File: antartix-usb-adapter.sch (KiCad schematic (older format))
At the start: 118 parts, among them IC1 FT2232D, J1 QTE-020-04-L-D-A, J2 0022232041, J3 614004185023, J4 WE_629105150521, J5 614004185023, J6 614004185023, U1 PCT2075GVX, U2 PAC1934T-I_JQ, U3 USB2514B-I_M2, U4 TPS2024DR, U5 TPS2024DR, U6 TPS2024DR, Y1 7C-24.000MBB-T, Y2 MQ-6.000-12-30_30_

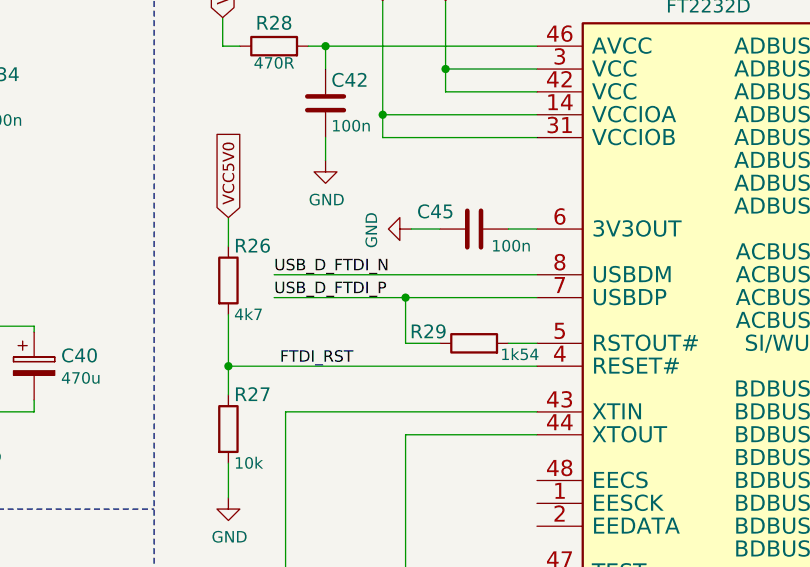
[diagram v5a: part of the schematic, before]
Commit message: Route console and HDMI control signals
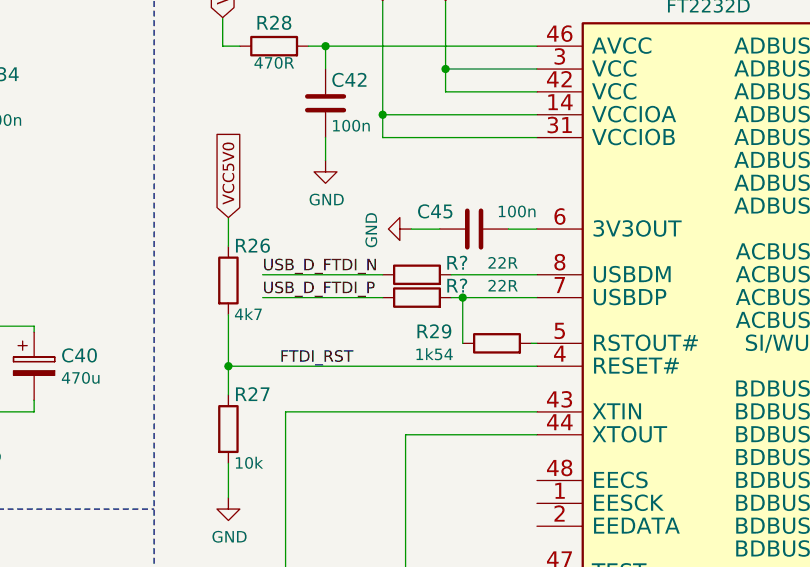
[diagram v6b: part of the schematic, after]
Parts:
- added R? (x2): R_22R_0402, antartix-arty-controller-footprints:0402-res, symbol antartix-arty-controller:R_22R_0402
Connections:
- net USB_D_FTDI_N: now also R?.1; no longer IC1.8 (USBDM)
- net USB_D_FTDI_P: now also R?.1; no longer IC1.7 (USBDP), R29.1
- new net: IC1.8 (USBDM), R?.2
- new net: IC1.7 (USBDP), R29.1, R?.2
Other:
- moved on the sheet: R29
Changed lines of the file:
@@
 $EndComp
 Wire Wire Line
-	12800 7650 12650 7650
-Wire Wire Line
-	12650 7450 12075 7450
-Connection ~ 12650 7450
-Wire Wire Line
-	12650 7650 12650 7450
-Wire Wire Line
-	13225 7650 13100 7650
+	13225 7650 13200 7650
 $Comp
 L antartix-arty-controller:R_1k54_0402 R?
 U 1 1 60939406
-P 12950 7650
+P 13050 7650
 AR Path="/60939406" Ref="R?"  Part="1"
 AR Path="/60924187/60939406" Ref="R29"  Part="1"
-F 0 "R29" H 12750 7700 60  0000 C CNN
-F 1 "R_1k54_0402" H 12950 7500 60  0001 C CNN
-F 2 "antartix-arty-controller-footprints:0402-res" H 13150 7850 60  0001 L CNN
-F 3 "" H 12950 7650 50  0001 C CNN
-F 4 "VISHAY" H 13150 8050 60  0001 L CNN "Manufacturer"
-F 5 "CRCW04021K54FKED." H 13150 7950 60  0001 L CNN "MPN"
-F 6 "1k54" H 13150 7600 50  0000 C CNN "Val"
-	1    12950 7650
+F 0 "R29" H 12775 7700 60  0000 C CNN
+F 1 "R_1k54_0402" H 13050 7500 60  0001 C CNN
+F 2 "antartix-arty-controller-footprints:0402-res" H 13250 7850 60  0001 L CNN
+F 3 "" H 13050 7650 50  0001 C CNN
+F 4 "VISHAY" H 13250 8050 60  0001 L CNN "Manufacturer"
+F 5 "CRCW04021K54FKED." H 13250 7950 60  0001 L CNN "MPN"
+F 6 "1k54" H 12775 7600 50  0000 C CNN "Val"
+	1    13050 7650
 	1    0    0    -1
 $EndComp
@@
 F 4 "Walsin" H 13150 7550 60  0001 L CNN "Manufacturer"
 F 5 "0402X104K6R3CT" H 13150 7450 60  0001 L CNN "MPN"
-F 6 "100n" V 13025 7225 50  0000 L CNN "Val"
+F 6 "100n" V 12875 7250 50  0000 L CNN "Val"
 	1    12950 7150
 	0    1    1    0
@@
 Wire Wire Line
 	14725 6450 14825 6450
-Text Label 12075 7450 0    50   ~ 0
+Text Label 12025 7450 0    50   ~ 0
 USB_D_FTDI_P
-Wire Wire Line
-	13225 7450 12650 7450
-Text Label 12075 7350 0    50   ~ 0
+Text Label 12025 7350 0    50   ~ 0
 USB_D_FTDI_N
-Wire Wire Line
-	13225 7350 12075 7350
 Text Label 15750 6650 2    50   ~ 0
 WP_FTDI
@@
 	1    0    0    -1
 $EndComp
+$Comp
+L antartix-arty-controller:R_22R_0402 R?
+U 1 1 605E94E5
+P 12700 7350
+AR Path="/604C47E1/605E94E5" Ref="R?"  Part="1"
+AR Path="/60924187/605E94E5" Ref="R?"  Part="1"
+F 0 "R?" H 12875 7400 60  0000 C CNN
+F 1 "R_22R_0402" H 12700 7200 60  0001 C CNN
+F 2 "antartix-arty-controller-footprints:0402-res" H 12900 7550 60  0001 L CNN
+F 3 "" H 12700 7350 50  0001 C CNN
+F 4 "VISHAY" H 12900 7750 60  0001 L CNN "Manufacturer"
+F 5 "CRCW040222R0FKED" H 12900 7650 60  0001 L CNN "MPN"
+F 6 "22R" H 13075 7400 50  0000 C CNN "Val"
+	1    12700 7350
+	1    0    0    -1
+$EndComp
+Wire Wire Line
+	12850 7450 12900 7450
+$Comp
+L antartix-arty-controller:R_22R_0402 R?
+U 1 1 605E94EE
+P 12700 7450
+AR Path="/604C47E1/605E94EE" Ref="R?"  Part="1"
+AR Path="/60924187/605E94EE" Ref="R?"  Part="1"
+F 0 "R?" H 12875 7500 60  0000 C CNN
+F 1 "R_22R_0402" H 12700 7300 60  0001 C CNN
+F 2 "antartix-arty-controller-footprints:0402-res" H 12900 7650 60  0001 L CNN
+F 3 "" H 12700 7450 50  0001 C CNN
+F 4 "VISHAY" H 12900 7850 60  0001 L CNN "Manufacturer"
+F 5 "CRCW040222R0FKED" H 12900 7750 60  0001 L CNN "MPN"
+F 6 "22R" H 13075 7500 50  0000 C CNN "Val"
+	1    12700 7450
+	1    0    0    -1
+$EndComp
+Wire Wire Line
+	12900 7650 12900 7450
+Connection ~ 12900 7450
+Wire Wire Line
+	12900 7450 13225 7450
+Wire Wire Line
+	12850 7350 13225 7350
+Wire Wire Line
+	12550 7350 12025 7350
+Wire Wire Line
+	12550 7450 12025 7450
 $EndSCHEMATC

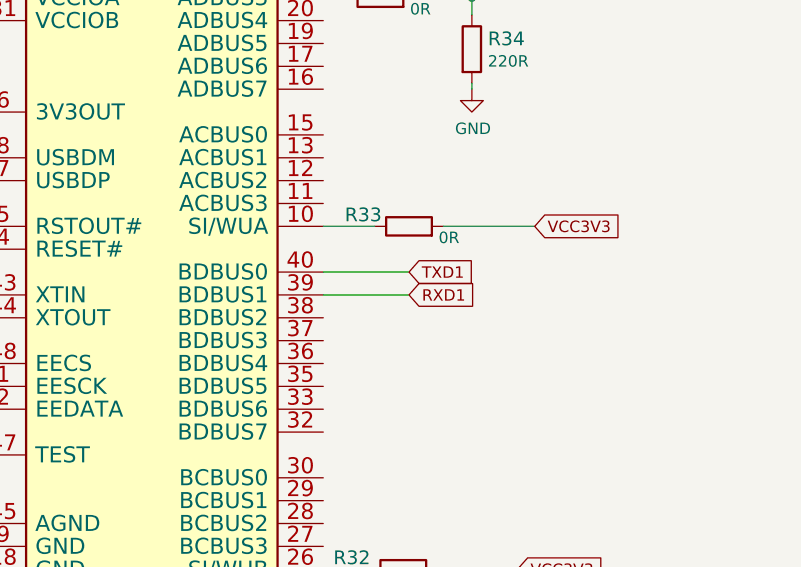
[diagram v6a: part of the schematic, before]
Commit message: Remove TXD1 and RXD1 labels
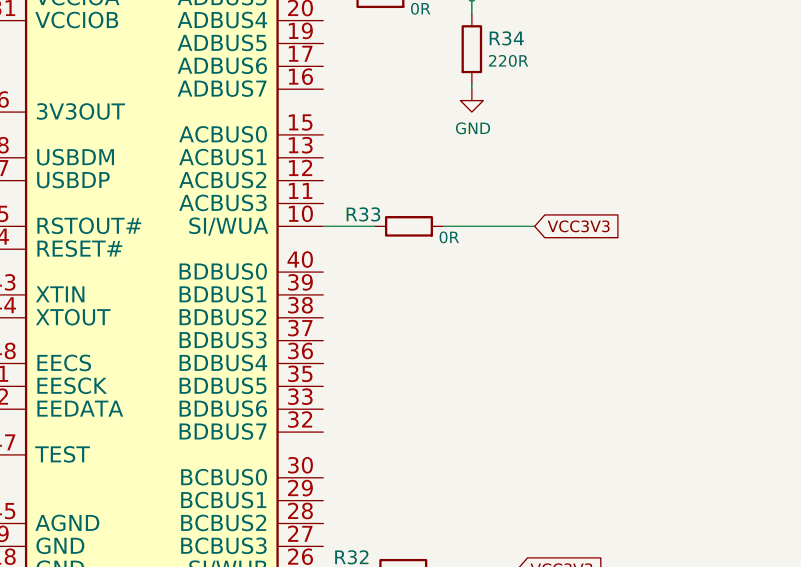
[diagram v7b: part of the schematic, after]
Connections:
- net RXD1: no longer names the net of IC1.39 (BDBUS1)
- net TXD1: no longer names the net of IC1.40 (BDBUS0)
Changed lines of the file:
@@
 	1    0    0    -1
 $EndComp
-Text GLabel 15100 7850 2    50   Input ~ 0
-TXD1
-Text GLabel 15100 7950 2    50   Input ~ 0
-RXD1
-Wire Wire Line
-	15100 7850 14725 7850
-Wire Wire Line
-	15100 7950 14725 7950
 Text GLabel 3200 2375 2    50   Input ~ 0
 USB1_EN

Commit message: Add local libraries
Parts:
- C10, C11, C12: footprint antmicro-footprints:0603-cap -> antartix-arty-controller-footprints:0603-cap; symbol antmicroCapacitors0603:C_100n_0603 -> antartix-arty-controller:C_100n_0603
- C13: footprint antmicro-footprints:0402-cap -> antartix-arty-controller-footprints:0402-cap; symbol antmicroCapacitors0402:C_1u_0402 -> antartix-arty-controller:C_1u_0402
- C37, C38, C39: footprint antmicro-footprints:0603-cap -> antartix-arty-controller-footprints:0603-cap; symbol antmicroCapacitors0603:C_22u_0603 -> antartix-arty-controller:C_22u_0603
- J2: footprint antmicro-footprints:PinHeader_1x4_P2.54mm_Drill1.02mm -> antartix-arty-controller-footprints:PinHeader_1x4_P2.54mm_Drill1.02mm
- J3, J5, J6: symbol antmicroUSBDVIHDMIConnectors:614004185023 -> antartix-arty-controller:614004185023
- N1: footprint antmicro-footprints:antmicro-logo_scaled_15mm -> antartix-arty-controller-footprints:antmicro-logo_scaled_15mm; symbol antmicroMechanicalParts:antmicro_logo -> antartix-arty-controller:antmicro_logo
- N2: footprint antmicro-footprints:oshw-logo -> antartix-arty-controller-footprints:oshw-logo; symbol antmicroMechanicalParts:oshw_logo -> antartix-arty-controller:oshw_logo
- R25: footprint antmicro-footprints:0402-res -> antartix-arty-controller-footprints:0402-res; symbol antmicroResistors0402:R_12k_0402 -> antartix-arty-controller:R_12k_0402
- R3, R4: footprint antmicro-footprints:0805-res -> antartix-arty-controller-footprints:0805-res; symbol antmicroResistorsmisc:R_0R_0805 -> antartix-arty-controller:R_0R_0805
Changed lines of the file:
@@
 F 0 "J2" V 6925 7308 50  0000 C CNN
 F 1 "0022232041" V 7016 7308 50  0000 C CNN
-F 2 "antmicro-footprints:PinHeader_1x4_P2.54mm_Drill1.02mm" H 7350 7500 60  0001 L CNN
+F 2 "antartix-arty-controller-footprints:PinHeader_1x4_P2.54mm_Drill1.02mm" H 7350 7500 60  0001 L CNN
 F 3 "https://www.molex.com/pdm_docs/sd/022232041_sd.pdf" H 7350 7600 60  0001 L CNN
 F 4 "0022232041" H 7350 7800 60  0001 L CNN "MPN"
@@
 VCC3V3
 $Comp
-L antmicroCapacitors0402:C_1u_0402 C?
+L antartix-arty-controller:C_1u_0402 C?
 U 1 1 60938EAE
 P 9000 6575
@@
 F 0 "C13" H 9025 6675 60  0000 L CNN
 F 1 "C_1u_0402" H 9000 6425 60  0001 C CNN
-F 2 "antmicro-footprints:0402-cap" H 9200 6775 60  0001 L CNN
+F 2 "antartix-arty-controller-footprints:0402-cap" H 9200 6775 60  0001 L CNN
 F 3 "" H 9000 6575 50  0001 C CNN
 F 4 "TDK" H 9200 6975 60  0001 L CNN "Manufacturer"
@@
 $EndComp
 $Comp
-L antmicroCapacitors0603:C_100n_0603 C?
+L antartix-arty-controller:C_100n_0603 C?
 U 1 1 60938F63
 P 9000 3550
@@
 F 0 "C12" H 8775 3625 60  0000 L CNN
 F 1 "C_100n_0603" H 9000 3400 60  0001 C CNN
-F 2 "antmicro-footprints:0603-cap" H 9200 3750 60  0001 L CNN
+F 2 "antartix-arty-controller-footprints:0603-cap" H 9200 3750 60  0001 L CNN
 F 3 "" H 9000 3550 50  0001 C CNN
 F 4 "AVX" H 9200 3950 60  0001 L CNN "Manufacturer"
@@
 $EndComp
 $Comp
-L antmicroCapacitors0603:C_22u_0603 C?
+L antartix-arty-controller:C_22u_0603 C?
 U 1 1 60938F8D
 P 10975 3500
@@
 F 0 "C39" H 10775 3400 60  0000 L CNN
 F 1 "C_22u_0603" H 10975 3350 60  0001 C CNN
-F 2 "antmicro-footprints:0603-cap" H 11175 3700 60  0001 L CNN
+F 2 "antartix-arty-controller-footprints:0603-cap" H 11175 3700 60  0001 L CNN
 F 3 "" H 10975 3500 50  0001 C CNN
 F 4 "MURATA" H 11175 3900 60  0001 L CNN "Manufacturer"
@@
 $EndComp
 $Comp
-L antmicroCapacitors0603:C_100n_0603 C?
+L antartix-arty-controller:C_100n_0603 C?
 U 1 1 60938FAF
 P 9000 2525
@@
 F 0 "C11" H 8775 2600 60  0000 L CNN
 F 1 "C_100n_0603" H 9000 2375 60  0001 C CNN
-F 2 "antmicro-footprints:0603-cap" H 9200 2725 60  0001 L CNN
+F 2 "antartix-arty-controller-footprints:0603-cap" H 9200 2725 60  0001 L CNN
 F 3 "" H 9000 2525 50  0001 C CNN
 F 4 "AVX" H 9200 2925 60  0001 L CNN "Manufacturer"
@@
 $EndComp
 $Comp
-L antmicroCapacitors0603:C_22u_0603 C?
+L antartix-arty-controller:C_22u_0603 C?
 U 1 1 60938FD9
 P 10975 2475
@@
 F 0 "C38" H 10775 2375 60  0000 L CNN
 F 1 "C_22u_0603" H 10975 2325 60  0001 C CNN
-F 2 "antmicro-footprints:0603-cap" H 11175 2675 60  0001 L CNN
+F 2 "antartix-arty-controller-footprints:0603-cap" H 11175 2675 60  0001 L CNN
 F 3 "" H 10975 2475 50  0001 C CNN
 F 4 "MURATA" H 11175 2875 60  0001 L CNN "Manufacturer"
@@
 $EndComp
 $Comp
-L antmicroCapacitors0603:C_100n_0603 C?
+L antartix-arty-controller:C_100n_0603 C?
 U 1 1 60938FFC
 P 9000 1525
@@
 F 0 "C10" H 8775 1600 60  0000 L CNN
 F 1 "C_100n_0603" H 9000 1375 60  0001 C CNN
-F 2 "antmicro-footprints:0603-cap" H 9200 1725 60  0001 L CNN
+F 2 "antartix-arty-controller-footprints:0603-cap" H 9200 1725 60  0001 L CNN
 F 3 "" H 9000 1525 50  0001 C CNN
 F 4 "AVX" H 9200 1925 60  0001 L CNN "Manufacturer"
@@
 	5300 10475 4725 10475
 $Comp
-L antmicroMechanicalParts:oshw_logo N?
+L antartix-arty-controller:oshw_logo N?
 U 1 1 6093902F
 P 1875 10925
@@
 F 0 "N2" H 2069 10928 50  0000 L CNN
 F 1 "oshw_logo" H 2069 10837 50  0000 L CNN
-F 2 "antmicro-footprints:oshw-logo" H 1895 10685 50  0001 C CNN
+F 2 "antartix-arty-controller-footprints:oshw-logo" H 1895 10685 50  0001 C CNN
 F 3 "" H 1875 10925 50  0001 C CNN
 	1    1875 10925
@@
 $EndComp
 $Comp
-L antmicroMechanicalParts:antmicro_logo N?
+L antartix-arty-controller:antmicro_logo N?
 U 1 1 60939035
 P 950 11025
@@
 F 0 "N1" H 1164 11118 50  0000 L CNN
 F 1 "antmicro_logo" H 1164 11027 50  0000 L CNN
-F 2 "antmicro-footprints:antmicro-logo_scaled_15mm" H 850 11275 50  0001 C CNN
+F 2 "antartix-arty-controller-footprints:antmicro-logo_scaled_15mm" H 850 11275 50  0001 C CNN
 F 3 "" H 950 11375 50  0001 C CNN
 	1    950  11025
@@
 $EndComp
 $Comp
-L antmicroCapacitors0603:C_22u_0603 C?
+L antartix-arty-controller:C_22u_0603 C?
 U 1 1 60939065
 P 10975 1475
@@
 F 0 "C37" H 10775 1375 60  0000 L CNN
 F 1 "C_22u_0603" H 10975 1325 60  0001 C CNN
-F 2 "antmicro-footprints:0603-cap" H 11175 1675 60  0001 L CNN
+F 2 "antartix-arty-controller-footprints:0603-cap" H 11175 1675 60  0001 L CNN
 F 3 "" H 10975 1475 50  0001 C CNN
 F 4 "MURATA" H 11175 1875 60  0001 L CNN "Manufacturer"
@@
 	12225 2025 12300 2025
 $Comp
-L antmicroUSBDVIHDMIConnectors:614004185023 J?
+L antartix-arty-controller:614004185023 J?
 U 1 1 609390AE
 P 11825 1925
@@
 $EndComp
 $Comp
-L antmicroUSBDVIHDMIConnectors:614004185023 J?
+L antartix-arty-controller:614004185023 J?
 U 1 1 609390E8
 P 13325 1950
@@
 	7700 3350 7850 3350
 $Comp
-L antmicroResistors0402:R_12k_0402 R?
+L antartix-arty-controller:R_12k_0402 R?
 U 1 1 6093913F
 P 7850 3800
@@
 F 0 "R25" V 7895 3730 60  0000 R CNN
 F 1 "R_12k_0402" H 7850 3650 60  0001 C CNN
-F 2 "antmicro-footprints:0402-res" H 8050 4000 60  0001 L CNN
+F 2 "antartix-arty-controller-footprints:0402-res" H 8050 4000 60  0001 L CNN
 F 3 "" H 7850 3800 50  0001 C CNN
 F 4 "VISHAY" H 8050 4200 60  0001 L CNN "Manufacturer"
@@
 	1125 3275 900  3275
 $Comp
-L antmicroResistorsmisc:R_0R_0805 R?
+L antartix-arty-controller:R_0R_0805 R?
 U 1 1 60939155
 P 1275 3575
@@
 F 0 "R4" H 1150 3700 60  0000 C CNN
 F 1 "R_0R_0805" H 1275 3425 60  0001 C CNN
-F 2 "antmicro-footprints:0805-res" H 1475 3775 60  0001 L CNN
+F 2 "antartix-arty-controller-footprints:0805-res" H 1475 3775 60  0001 L CNN
 F 3 "" H 1275 3575 50  0001 C CNN
 F 4 "VISHAY" H 1475 3975 60  0001 L CNN "Manufacturer"
@@
 	15175 1650 15200 1650
 $Comp
-L antmicroUSBDVIHDMIConnectors:614004185023 J?
+L antartix-arty-controller:614004185023 J?
 U 1 1 609391B6
 P 14775 1950
@@
 USB3_EN
 $Comp
-L antmicroResistorsmisc:R_0R_0805 R?
+L antartix-arty-controller:R_0R_0805 R?
 U 1 1 6093915F
 P 1275 3275
@@
 F 0 "R3" H 1150 3375 60  0000 C CNN
 F 1 "R_0R_0805" H 1275 3125 60  0001 C CNN
-F 2 "antmicro-footprints:0805-res" H 1475 3475 60  0001 L CNN
+F 2 "antartix-arty-controller-footprints:0805-res" H 1475 3475 60  0001 L CNN
 F 3 "" H 1275 3275 50  0001 C CNN
 F 4 "VISHAY" H 1475 3675 60  0001 L CNN "Manufacturer"
